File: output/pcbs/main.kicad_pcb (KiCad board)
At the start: 2 copper layers, 140.4 x 111.9 mm, 43 parts

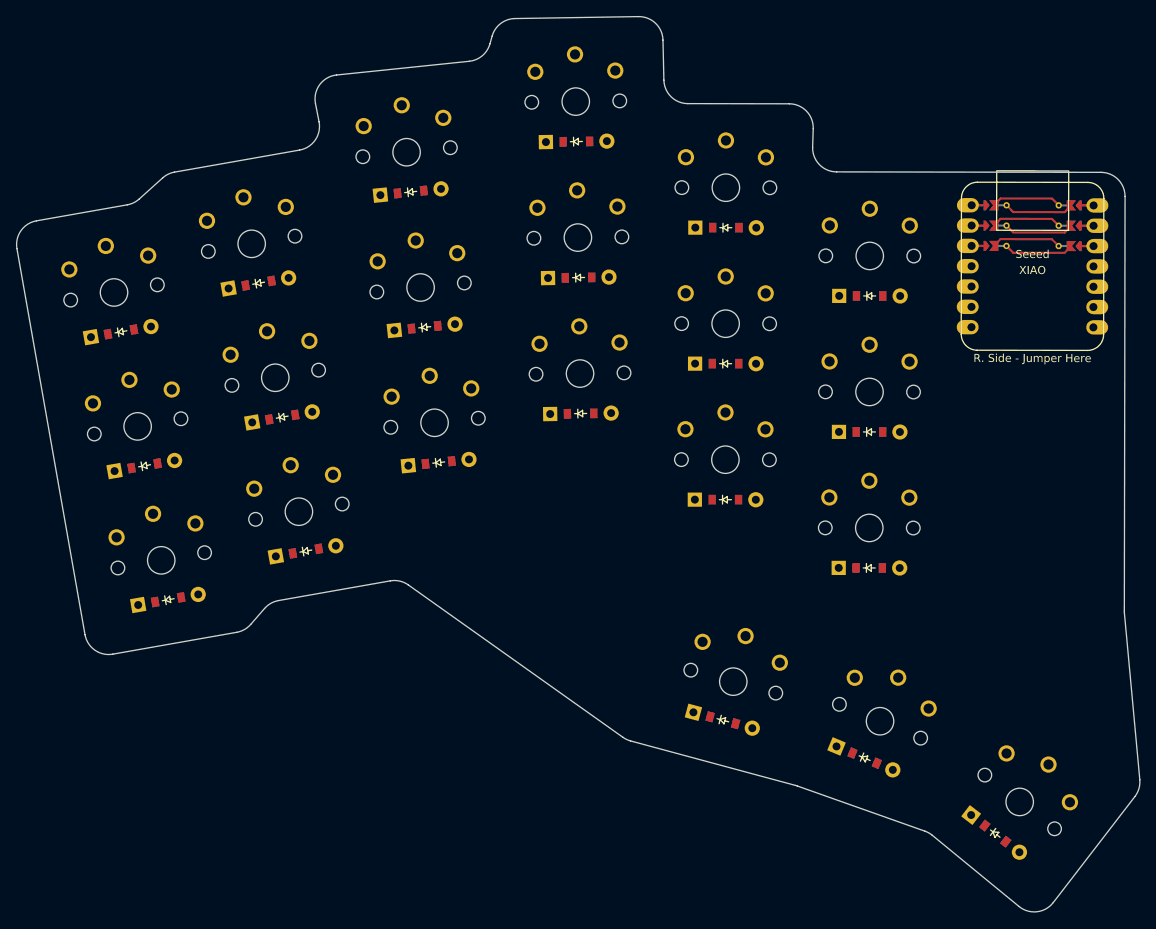
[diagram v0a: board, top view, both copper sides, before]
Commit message: added hotswap support
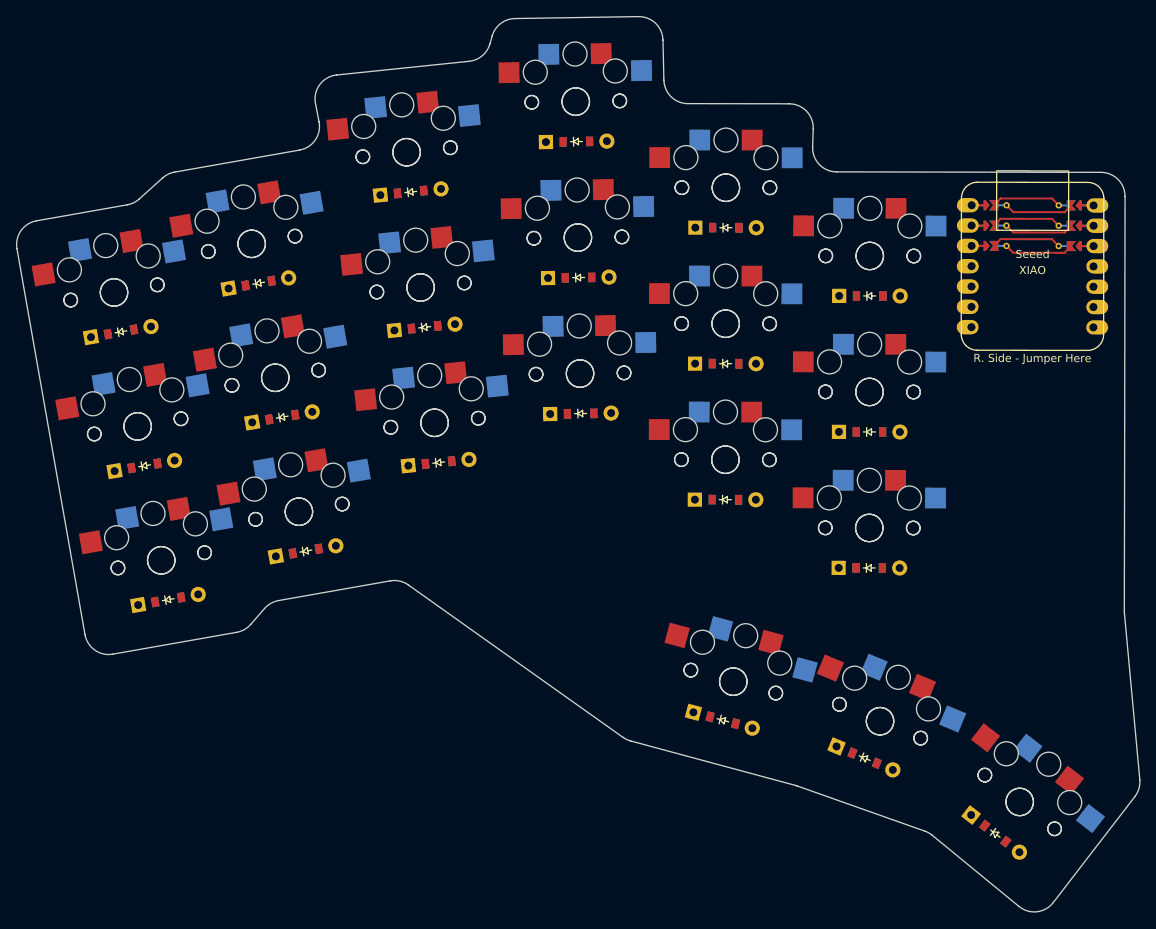
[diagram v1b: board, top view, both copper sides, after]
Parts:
- added N1: , PG1350, F.Cu at (100.0, 100.0)
- added N10: , PG1350, F.Cu at (152.3, 76.7)
- added N11: , PG1350, F.Cu at (152.1, 59.7)
- added N12: , PG1350, F.Cu at (151.8, 42.7)
- added N13: , PG1350, F.Cu at (170.5, 87.4)
- added N14: , PG1350, F.Cu at (170.5, 70.4)
- added N15: , PG1350, F.Cu at (170.6, 53.4)
- added N16: , PG1350, F.Cu at (188.5, 96.0)
- added N17: , PG1350, F.Cu at (188.5, 79.0)
- added N18: , PG1350, F.Cu at (188.6, 62.0)
- added N19: , PG1350, F.Cu at (171.5, 115.2)
- added N2: , PG1350, F.Cu at (97.0, 83.3)
- added N20: , PG1350, F.Cu at (189.8, 120.1)
- added N21: , PG1350, F.Cu at (207.3, 130.2)
- added N3: , PG1350, F.Cu at (94.1, 66.5)
- added N4: , PG1350, F.Cu at (117.2, 93.9)
- added N5: , PG1350, F.Cu at (114.3, 77.2)
- added N6: , PG1350, F.Cu at (111.3, 60.4)
- added N7: , PG1350, F.Cu at (134.2, 82.8)
- added N8: , PG1350, F.Cu at (132.4, 65.9)
- added N9: , PG1350, F.Cu at (130.7, 49.0)
